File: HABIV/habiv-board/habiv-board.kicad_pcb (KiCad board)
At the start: 4 copper layers, 100.3 x 120.9 mm, 115 parts, among them IC1 RTC_PCF8523T, J1 Micro_SD_Card_Det, J10 Conn_02x04_Counter_Clockwise, J2 Conn_ARM_JTAG_SWD_20, J3 Conn_01x02_Male, J4 Conn_01x16_Male, J5 Conn_01x02_Male, J6 Conn_01x16_Male, J7 Conn_01x16_Male, J8 Conn_02x04_Counter_Clockwise, J9 Conn_01x02_Male, Q1 32.768KHz, SW1 SW_DPST_x2, U1 STM32F401RET6, U2 MAX31855, U3 FGPMMOPA6H, U4 TPS564208, U5 TPS564208, U6 LSM9DS1TR, U7 MS560702BA03-00, Y1 32.768MHz

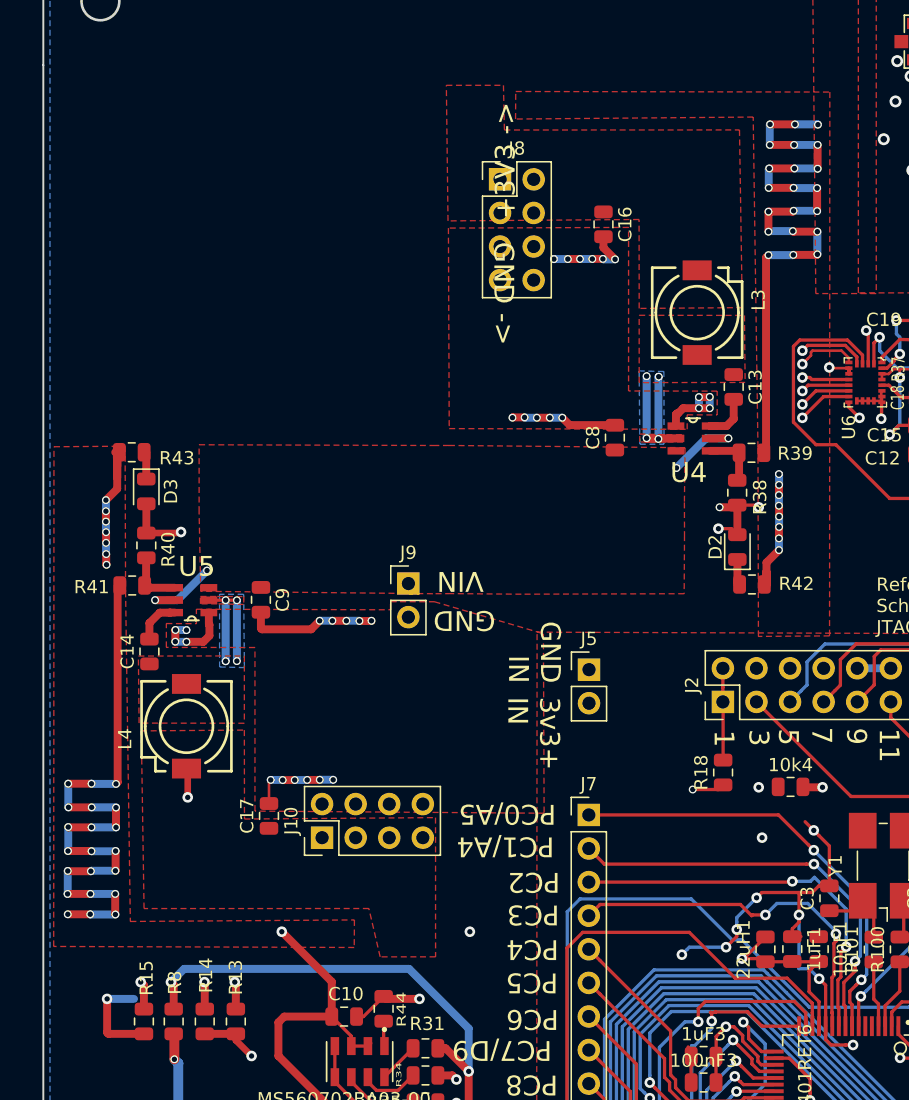
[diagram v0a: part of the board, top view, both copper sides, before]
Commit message: add xt30 connectors
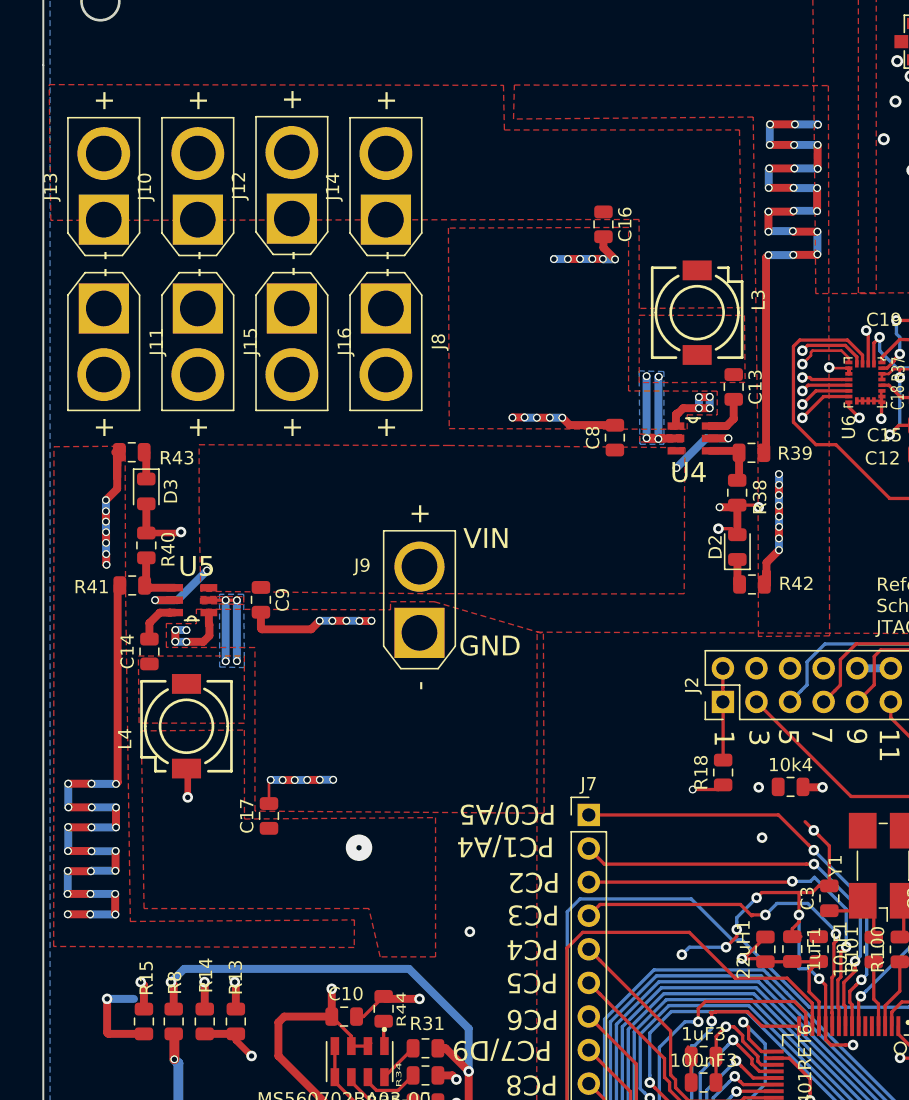
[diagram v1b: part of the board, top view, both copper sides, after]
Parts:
- removed J5: Conn_01x02_Male, Connector_PinHeader_2.54mm:PinHeader_1x02_P2.54mm_Vertical
- added J11: Conn_01x02_Female, Connector_AMASS:AMASS_XT30U-F_1x02_P5.0mm_Vertical, F.Cu at (85.6, 36.2)
- added J12: Conn_01x02_Female, Connector_AMASS:AMASS_XT30U-F_1x02_P5.0mm_Vertical, F.Cu at (99.8, 29.4)
- added J13: Conn_01x02_Female, Connector_AMASS:AMASS_XT30U-F_1x02_P5.0mm_Vertical, F.Cu at (85.6, 29.5)
- added J14: Conn_01x02_Female, Connector_AMASS:AMASS_XT30U-F_1x02_P5.0mm_Vertical, F.Cu at (106.9, 29.5)
- added J15: Conn_01x02_Female, Connector_AMASS:AMASS_XT30U-F_1x02_P5.0mm_Vertical, F.Cu at (92.7, 36.2)
- added J16: Conn_01x02_Female, Connector_AMASS:AMASS_XT30U-F_1x02_P5.0mm_Vertical, F.Cu at (99.8, 36.2)
- J10, J8: value Conn_02x04_Counter_Clockwise -> Conn_01x02_Female; footprint Connector_PinHeader_2.54mm:PinHeader_2x04_P2.54mm_Vertical -> Connector_AMASS:AMASS_XT30U-F_1x02_P5.0mm_Vertical
- J9: footprint Connector_PinHeader_2.54mm:PinHeader_1x02_P2.54mm_Vertical -> Connector_AMASS:AMASS_XT30U-M_1x02_P5.0mm_Vertical
- moved J10 47.7 mm to (92.7, 29.5)
- moved J8 13.0 mm to (106.9, 36.2), turned to 270 degrees
- moved J9 3.82 mm to (109.5, 60.7), turned to 90 degrees
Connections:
- J10 pad 1: +5V -> GND
- J10 pad 2: +5V -> +3V3
- J8 pad 1: +3V3 -> GND
- J8 pad 2: +3V3 -> +5V
- J9 pad 1: Net-(C8-Pad1) -> GND
- J9 pad 2: GND -> Net-(C8-Pad1)
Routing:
- net +5V: track 29.3 -> 88.6 mm, vias 2 -> 3
- net GND: track 422.4 -> 416.5 mm
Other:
- net class Default: trace_width 0.2 -> 2
- board text removed: "+3V3 ->"
- board text removed: "3v3+ IN"
- board text removed: "GND ->"
- board text removed: "GND IN"

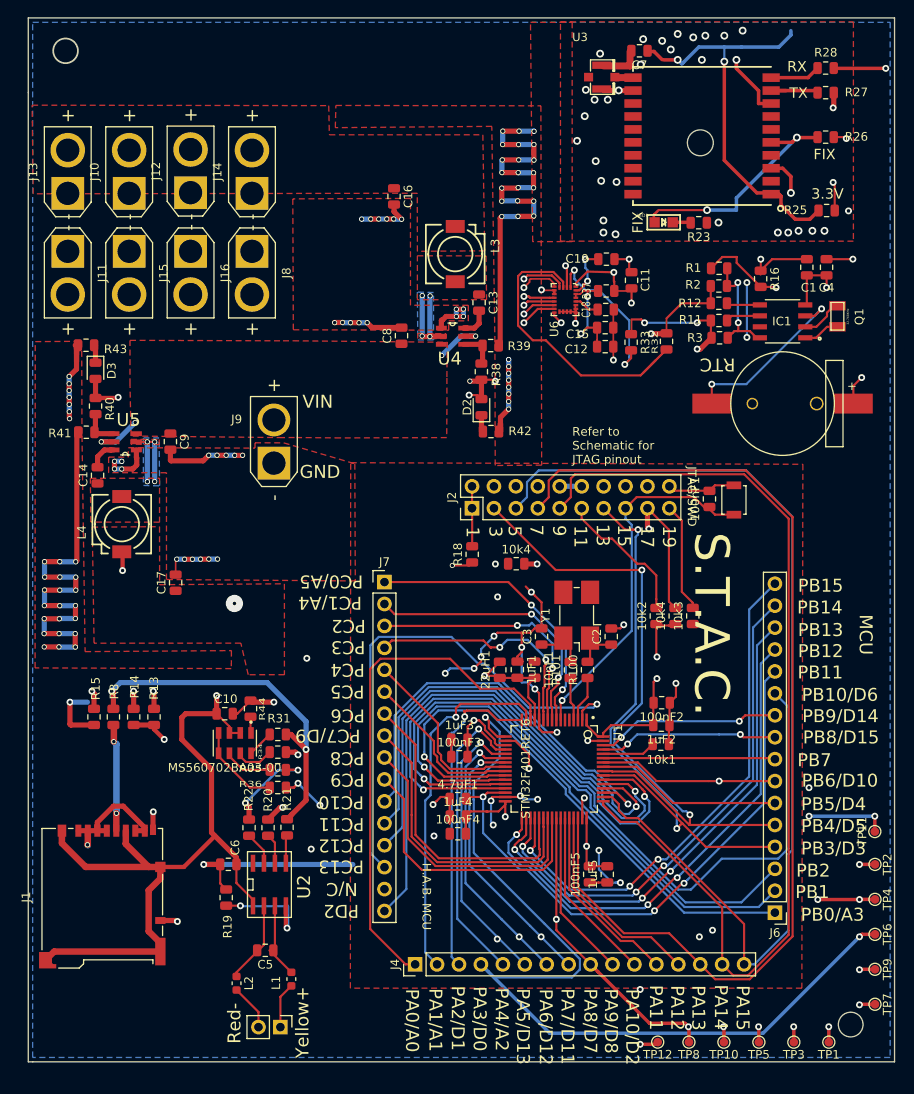
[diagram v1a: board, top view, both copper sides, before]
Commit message: clean up silkscreen
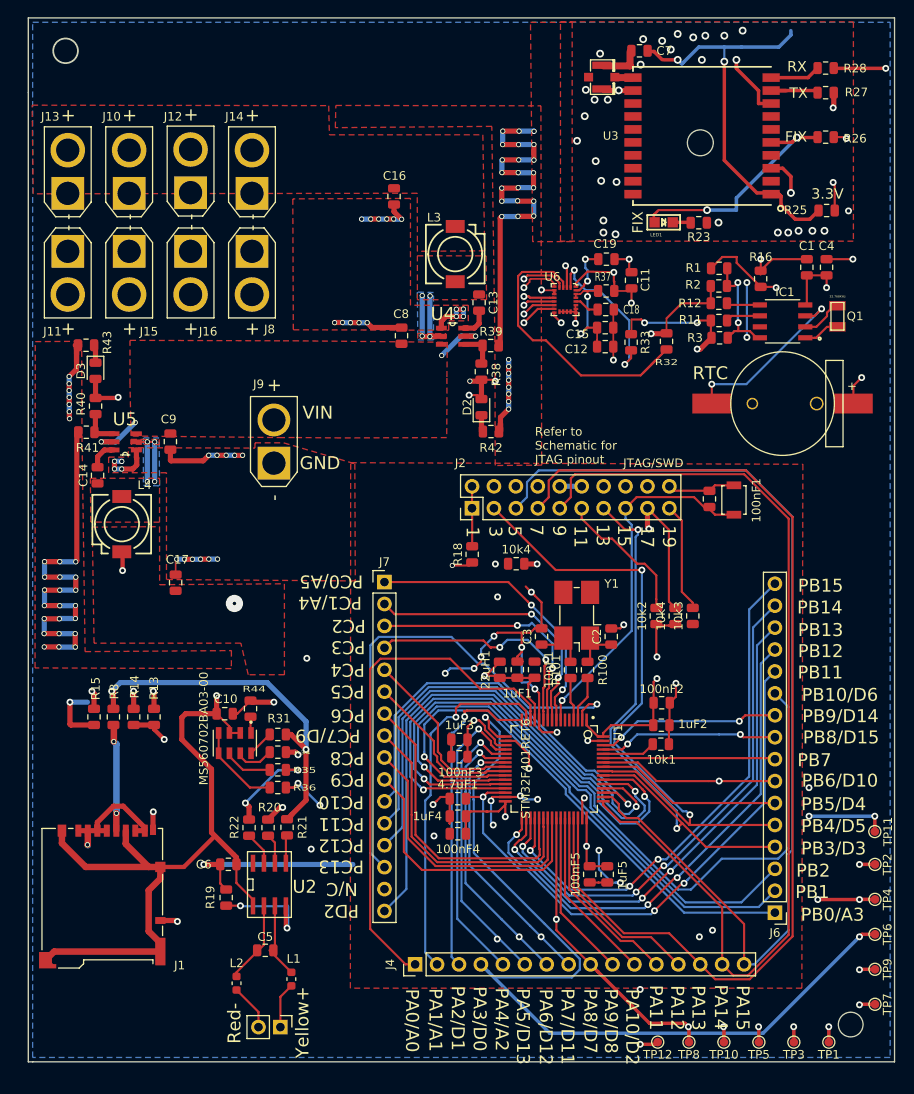
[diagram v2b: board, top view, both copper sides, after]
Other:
- board text removed: "H.A.B. MCU"
- board text removed: "MCU"
- board text removed: "S.T.A.C."

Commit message: add servo breakouts
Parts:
- added J17: Conn_01x03_Male, Connector_PinHeader_2.54mm:PinHeader_1x03_P2.54mm_Vertical, F.Cu at (121.9, 127.5)
- added J18: Conn_01x03_Male, Connector_PinHeader_2.54mm:PinHeader_1x03_P2.54mm_Vertical, F.Cu at (123.7, 12.2)
- added J19: Conn_01x03_Male, Connector_PinHeader_2.54mm:PinHeader_1x03_P2.54mm_Vertical, F.Cu at (123.7, 16.0)
- added J5: Conn_01x03_Male, Connector_PinHeader_2.54mm:PinHeader_1x03_P2.54mm_Vertical, F.Cu at (121.9, 123.6)
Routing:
- net PA10: track 20.3 -> 142.8 mm, vias 0 -> 1
- net PA11: track 22.0 -> 142.4 mm
- net +5V: track 88.6 -> 184.7 mm
- net +3V3: track 151.3 -> 134.0 mm
- net PA1: track 42.0 -> 53.4 mm
- net PA0: track 60.0 -> 65.4 mm
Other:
- outline, holes or cut-outs redrawn
- net class Default: trace_width 2 -> 0.5

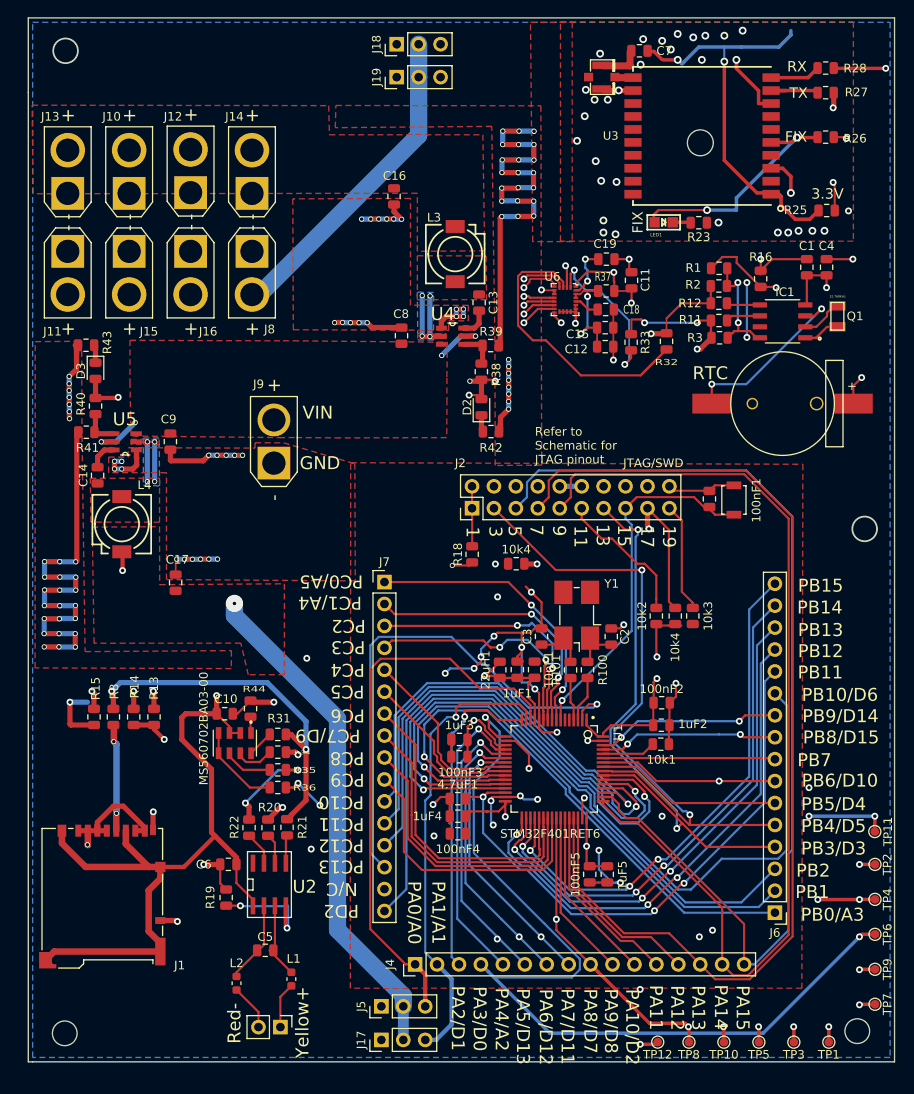
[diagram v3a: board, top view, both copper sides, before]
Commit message: add breakouts for rockblock and relay
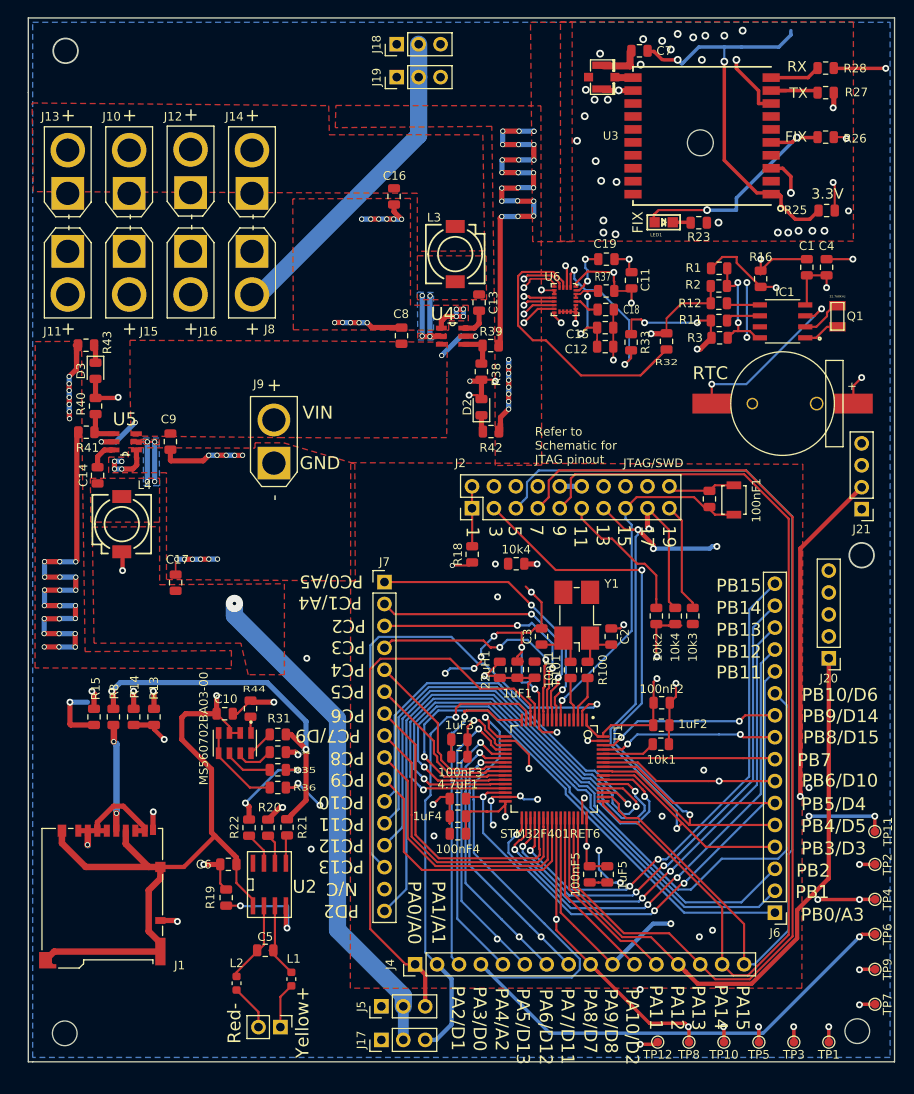
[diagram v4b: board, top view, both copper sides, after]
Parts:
- added J20: Conn_01x05_Male, Connector_PinHeader_2.54mm:PinHeader_1x05_P2.54mm_Vertical, F.Cu at (173.7, 83.3)
- added J21: Conn_01x04_Male, Connector_PinHeader_2.54mm:PinHeader_1x04_P2.54mm_Vertical, F.Cu at (177.5, 66.0)
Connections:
- J19 pad 3: PA11 -> PA9
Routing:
- net PA9: track 19.4 -> 143.7 mm, vias 0 -> 1
- net PA11: track 142.4 -> 69.7 mm, vias 0 -> 1
- net PA12: track 23.9 -> 74.8 mm
- net PB5: track 21.6 -> 63.6 mm, vias 0 -> 1
- net PB3: track 68.3 -> 99.4 mm, vias 2 -> 4
- net PB10: track 93.5 -> 105.3 mm
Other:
- outline, holes or cut-outs redrawn
